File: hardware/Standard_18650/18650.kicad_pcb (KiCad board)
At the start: 2 copper layers, 109.7 x 16 mm, 58 parts, among them J2 Battery, J3 GPIO, J4 USB_B_Micro, J5 Power, J6 LEDs, J7 GPIO, Q1 BSS806N, Q2 BSS806N, Q3 BSS806N, Q4 BSS806N, SW1 Mode, SW2 Power, U1 STM32F412CGUx, U2 AP2210N-3.3TRG1, U3 BQ21040, U4 ESD7002WTT1G, Y1 24Mhz

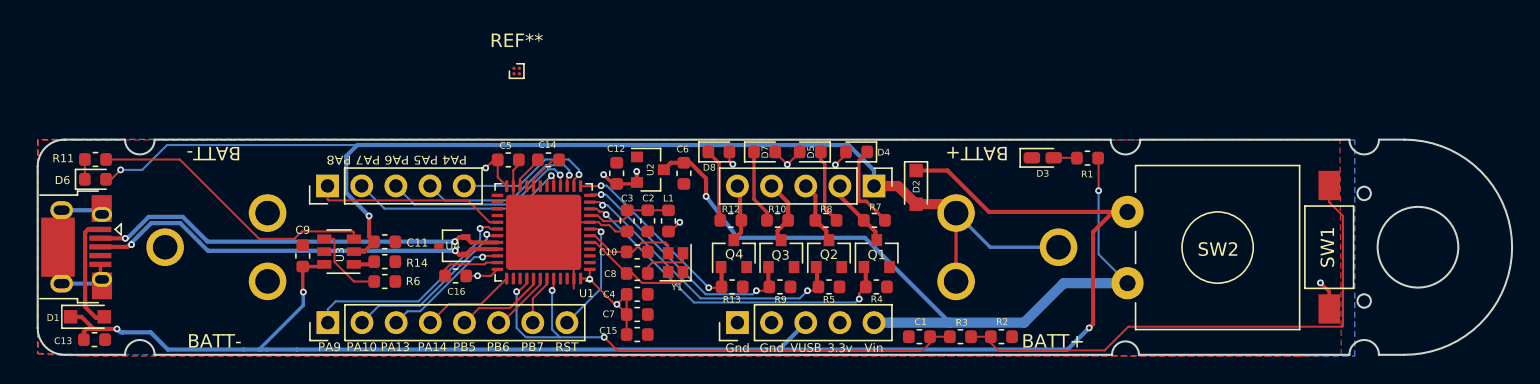
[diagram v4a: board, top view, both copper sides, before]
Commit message: Update pins and arduino examples.
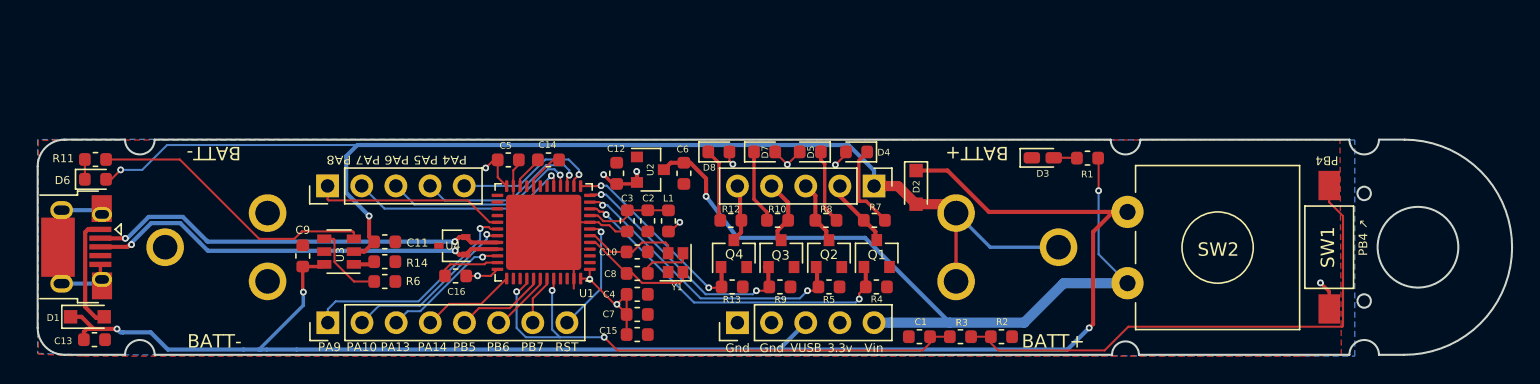
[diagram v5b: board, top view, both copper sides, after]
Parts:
- removed the REF** at (93.7, 86.9)
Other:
- board text added: "PB4"
- board text added: "PB4 ↗"
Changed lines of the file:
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@@
   (general
     (thickness 1.6)
-    (drawings 82)
+    (drawings 84)
     (tracks 455)
     (zones 0)
-    (modules 58)
+    (modules 57)
     (nets 45)
   )
@@
     (add_net "Net-(R6-Pad1)")
   )
-  (module Package_BGA:WLP-4_0.86x0.86mm_P0.4mm (layer F.Cu)
-    (at 93.725 86.9)
-    (descr "WLP-4_0.86x0.86mm_P0.4mm https://pdfserv.maximintegrated.com/package_dwgs/21-0612.PDF, https://www.maximintegrated.com/en/app-notes/index.mvp/id/1891")
-    (tags WLP-4)
-    (attr smd)
-    (fp_text reference REF** (at 0 -2.25) (layer F.SilkS)
-      (effects (font (size 1 1) (thickness 0.15)))
-    )
-    (fp_text value WLP-4_0.86x0.86mm_P0.4mm (at 0 2.25) (layer F.Fab)
-      (effects (font (size 1 1) (thickness 0.15)))
-    )
-    (fp_line (start -1.43 -1.43) (end 1.43 -1.43) (layer F.CrtYd) (width 0.05))
-    (fp_line (start -1.43 1.43) (end -1.43 -1.43) (layer F.CrtYd) (width 0.05))
-    (fp_line (start 1.43 1.43) (end -1.43 1.43) (layer F.CrtYd) (width 0.05))
-    (fp_line (start 1.43 -1.43) (end 1.43 1.43) (layer F.CrtYd) (width 0.05))
-    (fp_line (start 0.54 0.54) (end 0.54 -0.54) (layer F.SilkS) (width 0.12))
-    (fp_line (start -0.54 0.54) (end 0.54 0.54) (layer F.SilkS) (width 0.12))
-    (fp_line (start -0.54 0) (end -0.54 0.54) (layer F.SilkS) (width 0.12))
-    (fp_line (start 0.54 -0.54) (end 0 -0.54) (layer F.SilkS) (width 0.12))
-    (fp_line (start -0.17 -0.43) (end -0.43 -0.17) (layer F.Fab) (width 0.1))
-    (fp_line (start -0.43 -0.16) (end -0.43 0.43) (layer F.Fab) (width 0.1))
-    (fp_line (start 0.43 -0.43) (end -0.17 -0.43) (layer F.Fab) (width 0.1))
-    (fp_line (start 0.43 0.43) (end -0.43 0.43) (layer F.Fab) (width 0.1))
-    (fp_line (start 0.43 -0.43) (end 0.43 0.43) (layer F.Fab) (width 0.1))
-    (fp_text user %R (at 0 0) (layer F.Fab)
-      (effects (font (size 0.18 0.18) (thickness 0.045)))
-    )
-    (pad B2 smd circle (at 0.2 0.2) (size 0.25 0.25) (layers F.Cu F.Paste F.Mask))
-    (pad B1 smd circle (at -0.2 0.2) (size 0.25 0.25) (layers F.Cu F.Paste F.Mask))
-    (pad A2 smd circle (at 0.2 -0.2) (size 0.25 0.25) (layers F.Cu F.Paste F.Mask))
-    (pad A1 smd circle (at -0.2 -0.2) (size 0.25 0.25) (layers F.Cu F.Paste F.Mask))
-    (model ${KISYS3DMOD}/Package_BGA.3dshapes/WLP-4_0.86x0.86mm_P0.4mm.wrl
-      (at (xyz 0 0 0))
-      (scale (xyz 1 1 1))
-      (rotate (xyz 0 0 0))
-    )
-  )
   (module Diode_SMD:D_SOD-323_HandSoldering (layer F.Cu)
     (at 123.425 95.55 270)
@@
       (net 22 /PA4))
   )
+  (gr_text PB4 (at 153.975 93.55 180) (layer F.SilkS)
+    (effects (font (size 0.65 0.65) (thickness 0.1)))
+  )
+  (gr_text "PB4 ↗" (at 156.675 99.275 90) (layer F.SilkS)
+    (effects (font (size 0.65 0.65) (thickness 0.1)))
+  )
   (gr_text Gnd (at 110.14 103.925) (layer B.SilkS)
     (effects (font (size 0.65 0.65) (thickness 0.1)) (justify mirror))
@@
     (effects (font (size 0.65 0.65) (thickness 0.1)))
   )
-  (gr_text CLK (at 87.35 107.425) (layer B.SilkS)
+  (gr_text CLK (at 87.35 107.275) (layer B.SilkS)
     (effects (font (size 0.6 0.6) (thickness 0.1)) (justify mirror))
   )
-  (gr_text DIO (at 84.65 107.425) (layer B.SilkS)
+  (gr_text DIO (at 84.65 107.275) (layer B.SilkS)
     (effects (font (size 0.6 0.6) (thickness 0.1)) (justify mirror))
   )
-  (gr_text SCL (at 79.725 107.45) (layer B.SilkS)
+  (gr_text SCL (at 92.425 102.875) (layer B.SilkS)
     (effects (font (size 0.65 0.65) (thickness 0.1)) (justify mirror))
   )
-  (gr_text SDA (at 82.25 107.425) (layer B.SilkS)
+  (gr_text SDA (at 94.95 102.85) (layer B.SilkS)
     (effects (font (size 0.65 0.6) (thickness 0.1)) (justify mirror))
   )
@@
     (effects (font (size 0.65 0.6) (thickness 0.1)) (justify mirror))
   )
-  (gr_text TX (at 92.4 107.425) (layer B.SilkS)
+  (gr_text TX (at 92.4 107.275) (layer B.SilkS)
     (effects (font (size 0.65 0.65) (thickness 0.1)) (justify mirror))
   )
-  (gr_text RX (at 94.95 107.425) (layer B.SilkS)
+  (gr_text RX (at 94.95 107.275) (layer B.SilkS)
     (effects (font (size 0.65 0.65) (thickness 0.1)) (justify mirror))
   )
@@
   (gr_line (start 118.95 96.625) (end 104.55 96.625) (layer B.SilkS) (width 0.1))
   (gr_line (start 118.95 94.275) (end 118.95 96.625) (layer B.SilkS) (width 0.1))
-  (gr_text RST (at 97.45 103.825) (layer B.SilkS)
+  (gr_text RST (at 97.45 103.95) (layer B.SilkS)
     (effects (font (size 0.65 0.65) (thickness 0.1)) (justify mirror))
   )
-  (gr_text PB7 (at 94.95 103.825) (layer B.SilkS)
+  (gr_text PB7 (at 94.95 103.95) (layer B.SilkS)
     (effects (font (size 0.65 0.65) (thickness 0.1)) (justify mirror))
   )
-  (gr_text PB6 (at 92.4 103.825) (layer B.SilkS)
+  (gr_text PB6 (at 92.4 103.95) (layer B.SilkS)
     (effects (font (size 0.65 0.65) (thickness 0.1)) (justify mirror))
   )
@@
     (effects (font (size 0.65 0.65) (thickness 0.1)) (justify mirror))
   )
-  (gr_text PB5 (at 89.85 103.85) (layer B.SilkS)
+  (gr_text PB5 (at 89.85 103.975) (layer B.SilkS)
     (effects (font (size 0.65 0.65) (thickness 0.1)) (justify mirror))
   )
-  (gr_text PA14 (at 87.325 103.85) (layer B.SilkS)
+  (gr_text PA14 (at 87.325 103.975) (layer B.SilkS)
     (effects (font (size 0.65 0.6) (thickness 0.1)) (justify mirror))
   )
-  (gr_text PA13 (at 84.75 103.85) (layer B.SilkS)
+  (gr_text PA13 (at 84.75 103.975) (layer B.SilkS)
     (effects (font (size 0.65 0.6) (thickness 0.1)) (justify mirror))
   )
-  (gr_text PA10 (at 82.25 103.825) (layer B.SilkS)
+  (gr_text PA10 (at 82.25 103.95) (layer B.SilkS)
     (effects (font (size 0.65 0.6) (thickness 0.1)) (justify mirror))
   )
-  (gr_text PA9 (at 79.725 103.85) (layer B.SilkS)
+  (gr_text PA9 (at 79.725 103.975) (layer B.SilkS)
     (effects (font (size 0.65 0.65) (thickness 0.1)) (justify mirror))
   )

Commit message: Production boards.
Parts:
- R2: value 20K -> 20k
- R6: value 675 -> 680
- U1: value STM32F412CGUx -> STM32F411CE
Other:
- board text added: "rev 1.1"
- board text removed: "rev 1.1a2"

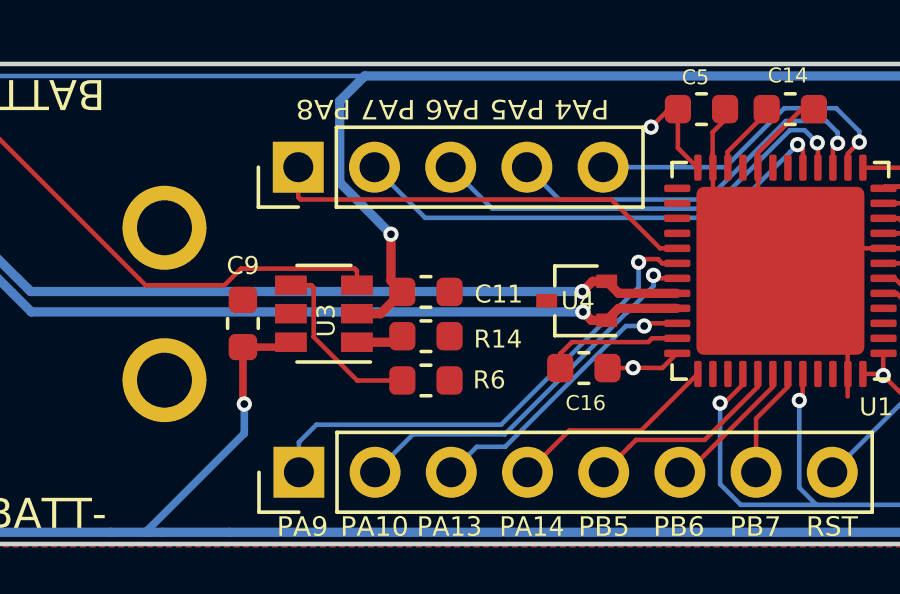
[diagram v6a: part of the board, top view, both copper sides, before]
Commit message: Add flash chip
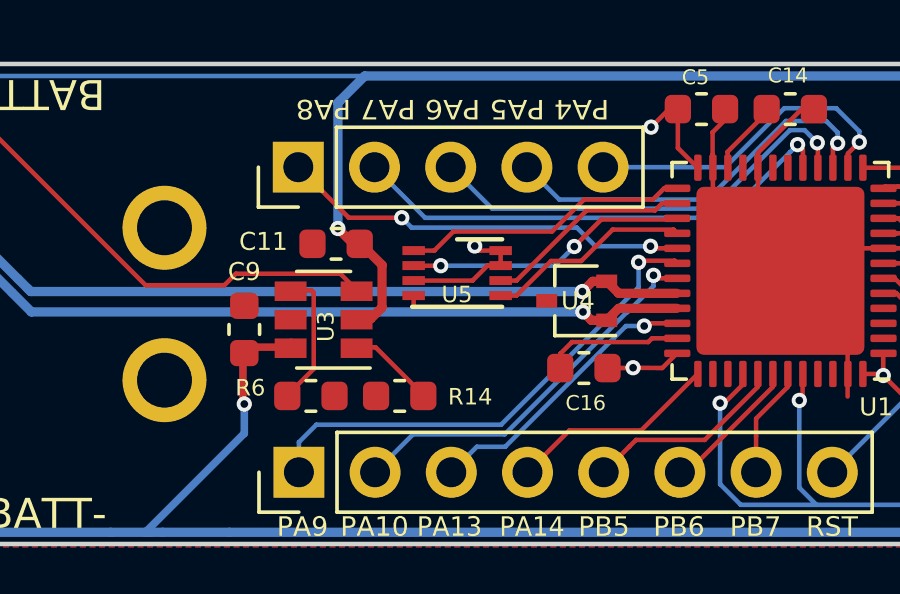
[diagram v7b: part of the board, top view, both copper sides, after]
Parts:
- added U5: GD25Q16CEIGR, Package_DFN_QFN:DFN-8-1EP_3x2mm_P0.5mm_EP1.3x1.5mm, F.Cu at (85.0, 99.0)
- moved R6 3.87 mm to (80.1, 103.1)
- moved C11 3.40 mm to (80.9, 98.0), turned to 180 degrees
- moved R14 2.17 mm to (83.0, 103.1), turned to 180 degrees
- moved C9 0.20 mm to (77.9, 100.8)
- moved U3 0.20 mm to (80.5, 100.5)
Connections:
- net /XTAL1 renamed Net-(C8-Pad1)
- net /XTAL2 renamed Net-(C10-Pad1)
- J4 pad 4: (no net) -> Net-(J4-Pad4)
- U1 pad 18: (no net) -> Net-(U1-Pad18)
- U1 pad 19: (no net) -> Net-(U1-Pad19)
- U1 pad 2: (no net) -> Net-(U1-Pad2)
- U1 pad 21: (no net) -> Net-(U1-Pad21)
- U1 pad 25: (no net) -> /FLASH_CSEL
- U1 pad 26: (no net) -> /FLASH_SCK
- U1 pad 27: (no net) -> /FLASH_MISO
- U1 pad 28: (no net) -> /FLASH_MOSI
- U1 pad 3: (no net) -> Net-(U1-Pad3)
- U1 pad 38: (no net) -> Net-(U1-Pad38)
- U1 pad 39: (no net) -> Net-(U1-Pad39)
- U1 pad 4: (no net) -> Net-(U1-Pad4)
- U1 pad 45: (no net) -> Net-(U1-Pad45)
- U1 pad 46: (no net) -> Net-(U1-Pad46)
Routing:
- net /FLASH_CSEL: track 0.00 -> 9.65 mm
- net /FLASH_MISO: track 0.00 -> 9.44 mm, vias 0 -> 2
- net /FLASH_SCK: track 0.00 -> 6.95 mm
- net /FLASH_MOSI: track 0.00 -> 6.85 mm
- net +3V3: track 27.2 -> 31.7 mm, vias 11 -> 12
- net Net-(R6-Pad1): track 5.99 -> 4.56 mm
- net Net-(R14-Pad1): track 1.60 -> 2.87 mm
- net /PA8: track 14.3 -> 13.8 mm, vias 0 -> 2

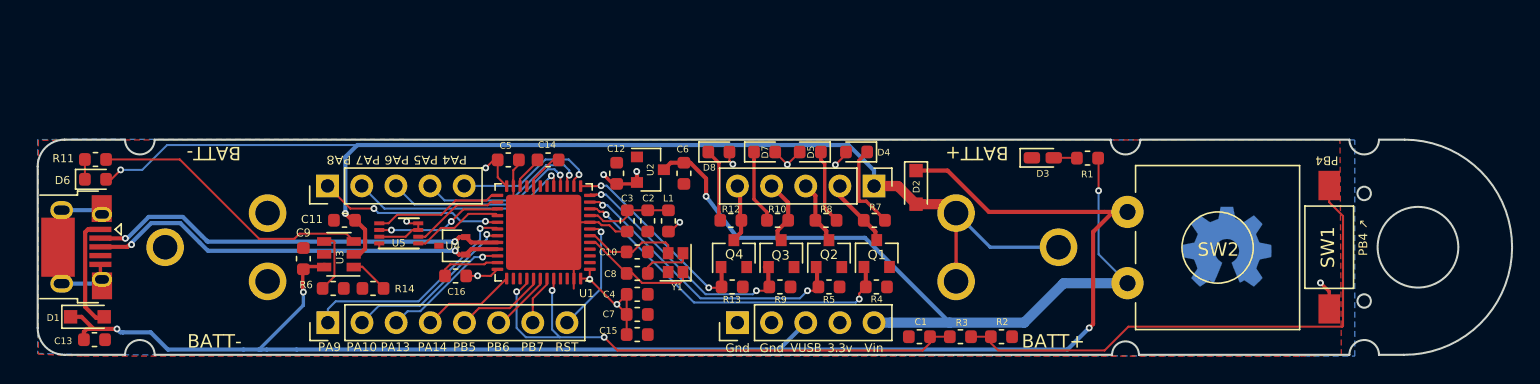
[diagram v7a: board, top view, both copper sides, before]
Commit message: Add RGB LED & Flash. Change power switch.
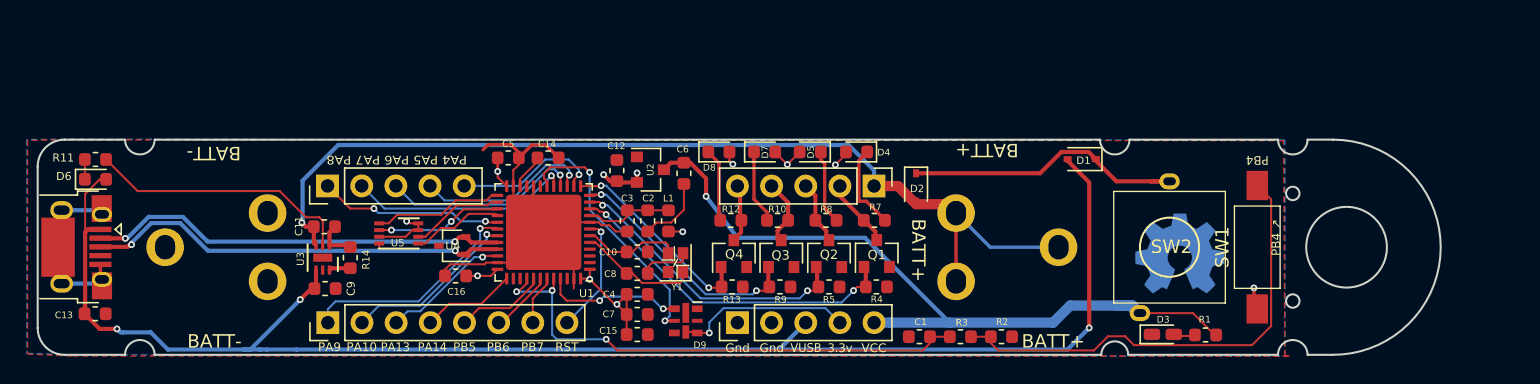
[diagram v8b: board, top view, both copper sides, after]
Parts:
- removed R6: 680, Resistor_SMD:R_0603_1608Metric
- added D9: APA102-2020, LED_SMD:LED-APA102-2020, F.Cu at (106.3, 105.5)
- C11, C9: value 1uF -> 4.7uF
- D1, D2: footprint Diode_SMD:D_SOD-323_HandSoldering -> Diode_SMD:D_SOD-323
- R14: value 10k -> 1k
- SW1: footprint Button_Switch_SMD:SW_SPST_FSMSM -> Jeremy Button/Switch:SW_SPST_FSMSM
- SW2: footprint Button_Switch_THT:SW_CW_GPTS203211B -> Jeremy:Switch_L068-A-DC30V1A
- U1: footprint Package_DFN_QFN:QFN-48-1EP_7x7mm_P0.5mm_EP5.6x5.6mm -> Jeremy:QFN-48-1EP_7x7mm_P0.5mm_EP5.6x5.6mm
- U3: value BQ21040 -> MCP73830; footprint Package_TO_SOT_SMD:SOT-23-6 -> Package_DFN_QFN:DFN-6-1EP_2x2mm_P0.5mm_EP0.61x1.42mm
- moved D1 74.9 mm to (135.8, 93.5), turned to 180 degrees
- moved D3 15.9 mm to (141.8, 106.5)
- moved R1 15.8 mm to (144.9, 106.5)
- moved SW1 5.35 mm to (148.8, 100.0)
- moved SW2 4.08 mm to (142.3, 100.0), turned to 180 degrees
- moved REF** 3.54 mm to (143.1, 100.5)
- moved R14 2.85 mm to (81.3, 100.8), turned to 90 degrees
- moved C9 2.75 mm to (79.5, 103.1), turned to 0 degrees
- moved C13 1.93 mm to (62.4, 105.0)
- moved C11 1.57 mm to (79.4, 98.5), turned to 0 degrees
- moved U3 1.23 mm to (79.3, 100.8), turned to 270 degrees
- moved C12 0.21 mm to (101.2, 94.3)
- moved C14 0.15 mm to (96.1, 93.4)
- moved C5 0.15 mm to (93.1, 93.4)
- turned R11 to 0 degrees
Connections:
- D1 pad 1: /VUSB -> Net-(D1-Pad1)
- D1 pad 2: Net-(D1-Pad2) -> /VUSB
- D2 pad 1: /VUSB -> Net-(D1-Pad1)
- D6 pad 2: +BATT -> /VUSB
- J4 pad 1: Net-(D1-Pad2) -> /VUSB
- J4 pad 4: Net-(J4-Pad4) -> (no net)
- R11 pad 1: Net-(R11-Pad1) -> Net-(D6-Pad1)
- R11 pad 2: Net-(D6-Pad1) -> Net-(R11-Pad2)
- SW2 pad 1: /VUSB -> Net-(D1-Pad1)
- U1 pad 18: Net-(U1-Pad18) -> /RGB_CKI
- U1 pad 19: Net-(U1-Pad19) -> (no net)
- U1 pad 2: Net-(U1-Pad2) -> (no net)
- U1 pad 21: Net-(U1-Pad21) -> (no net)
- U1 pad 3: Net-(U1-Pad3) -> (no net)
- U1 pad 38: Net-(U1-Pad38) -> (no net)
- U1 pad 39: Net-(U1-Pad39) -> (no net)
- U1 pad 4: Net-(U1-Pad4) -> (no net)
- U1 pad 45: Net-(U1-Pad45) -> /RGB_SDI
- U1 pad 46: Net-(U1-Pad46) -> (no net)
- U3 pad 1: Net-(R14-Pad1) -> GND
- U3 pad 2: +BATT -> Net-(R11-Pad2)
- U3 pad 3: Net-(R11-Pad1) -> +BATT
- U3 pad 4: Net-(R6-Pad1) -> /VUSB
- U3 pad 5: GND -> (no net)
- U3 pad 6: /VUSB -> Net-(R14-Pad1)
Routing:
- net Net-(D1-Pad1): track 0.00 -> 22.0 mm
- net Net-(R11-Pad1): track 21.3 -> 0.00 mm
- net Net-(R11-Pad2): track 0.00 -> 19.8 mm
- net /RGB_CKI: track 0.00 -> 19.1 mm, vias 0 -> 2
- net +BATT: track 90.6 -> 71.8 mm, vias 2 -> 1
- net GND: track 41.6 -> 58.7 mm
- net +3V3: track 31.7 -> 44.1 mm, vias 12 -> 13
- net /RGB_SDI: track 0.00 -> 10.3 mm, vias 0 -> 2
- net Net-(D1-Pad2): track 8.73 -> 0.00 mm
- net Net-(R2-Pad1): track 40.0 -> 35.2 mm
- net Net-(R6-Pad1): track 4.56 -> 0.00 mm
- net /VUSB: track 117.4 -> 113.3 mm
- net /BUTTON: track 42.5 -> 39.0 mm
- net Net-(R14-Pad1): track 2.87 -> 1.61 mm
- net /VIN: track 57.7 -> 57.5 mm, vias 2 -> 1
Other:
- board size 109.7 x 16 mm -> 104.3 x 16 mm
- board text added: "ThunderPack"
- board text added: "VCC"
- board text added: "v1.2a2"
- board text removed: "Thunder Pack"
- board text removed: "Vin"
- board text removed: "rev 1.1"
